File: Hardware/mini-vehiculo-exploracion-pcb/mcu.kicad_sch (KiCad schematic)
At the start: 19 parts, among them J2 USB_C_Receptacle_USB2.0_16P, SW1 SW_Push, SW2 SW_Push

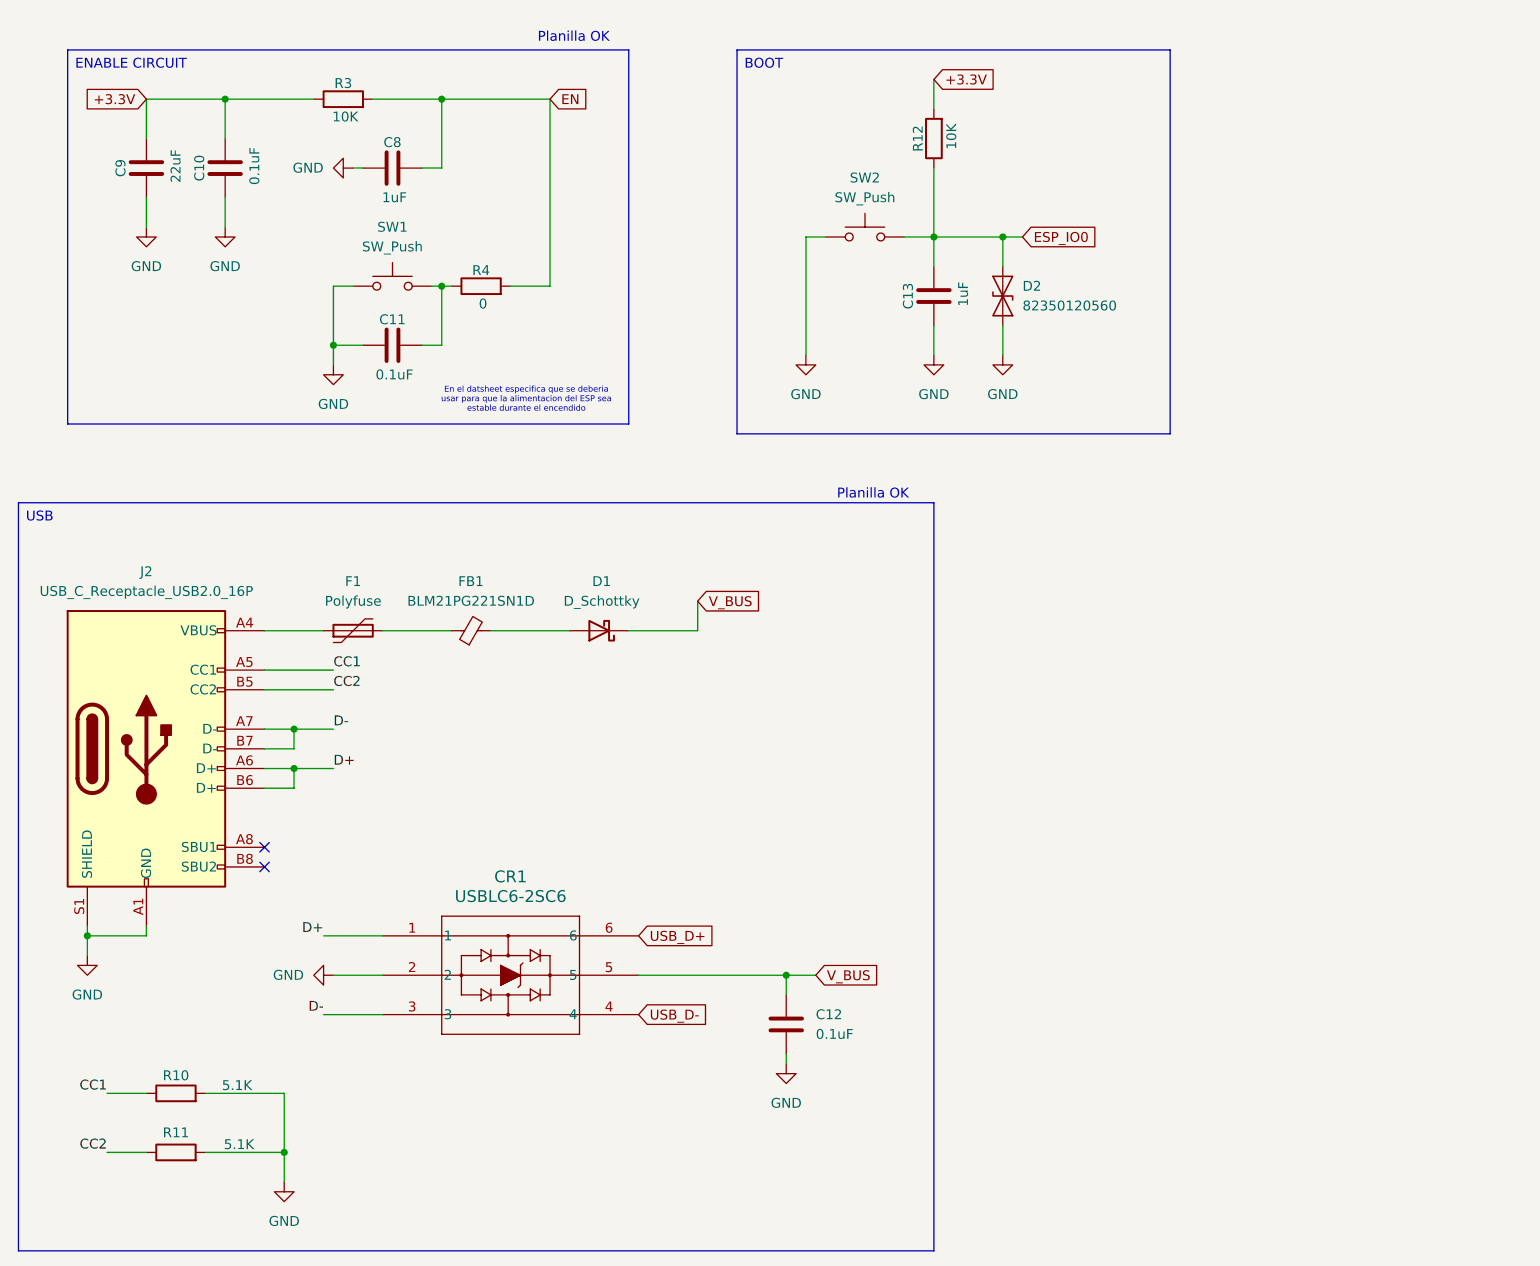
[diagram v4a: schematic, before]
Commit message: Add pin headers, run ERC
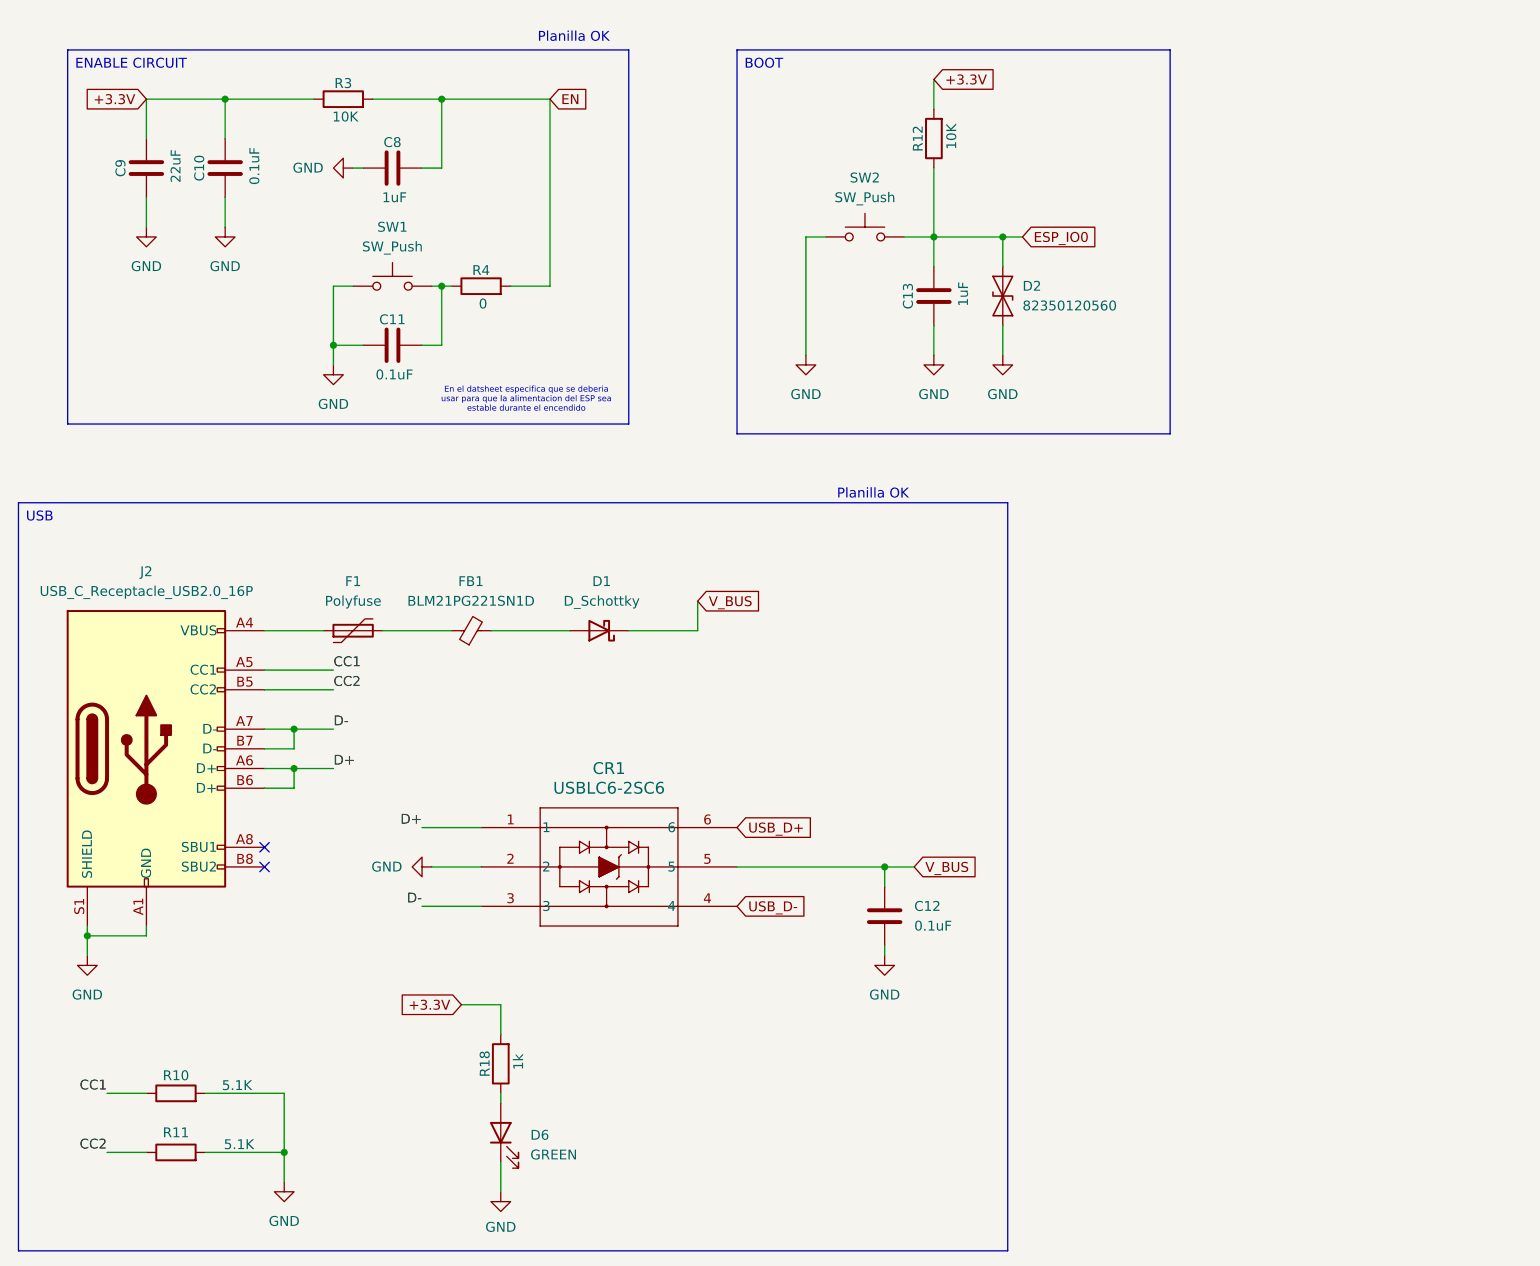
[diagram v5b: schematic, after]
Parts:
- added D6: GREEN, symbol Device:LED
- added R18: 1k, symbol Device:R
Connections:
- net +3.3V: now also R18.2
- net GND: now also D6.1 (K)
- new net: D6.2 (A), R18.1
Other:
- moved on the sheet: C12, CR1

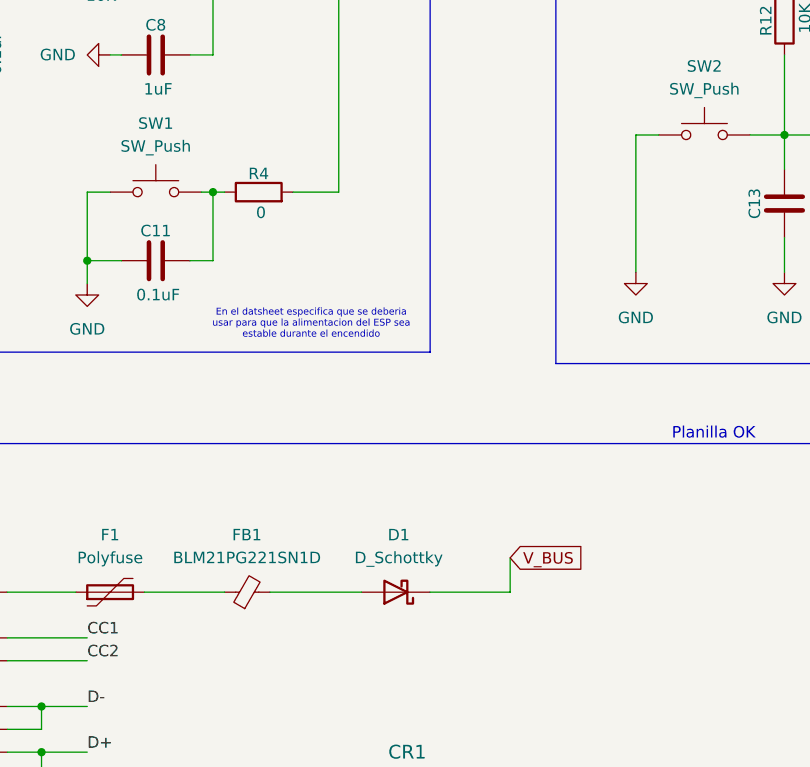
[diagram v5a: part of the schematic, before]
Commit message: Assigned NET CLASSES
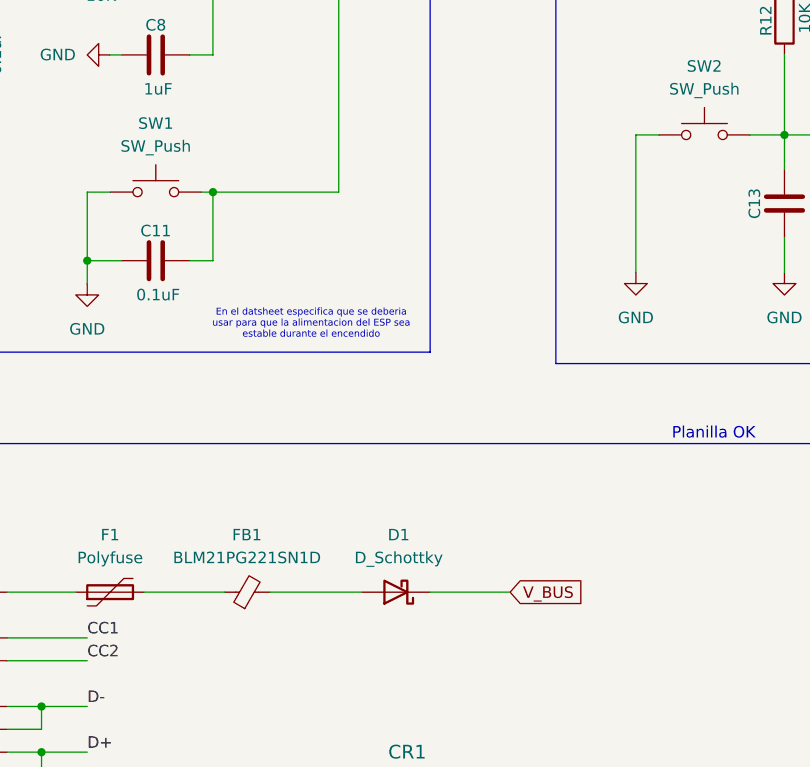
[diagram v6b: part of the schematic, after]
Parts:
- removed R4: 0, symbol Device:R
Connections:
- net EN: now also C11.2, SW1.2
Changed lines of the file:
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@@
-	(wire
-		(pts
-			(xy 110.49 101.6) (xy 110.49 97.79)
-		)
-		(stroke
-			(width 0)
-			(type default)
-		)
-	)
 	(wire
 		(pts
@@
 	(wire
 		(pts
-			(xy 86.36 57.15) (xy 91.44 57.15)
-		)
-		(stroke
-			(width 0)
-			(type default)
-		)
-	)
-	(wire
-		(pts
 			(xy 46.99 168.91) (xy 57.15 168.91)
 		)
@@
 	(wire
 		(pts
-			(xy 77.47 57.15) (xy 78.74 57.15)
+			(xy 77.47 57.15) (xy 91.44 57.15)
 		)
 		(stroke
@@
 	(global_label "V_BUS"
 		(shape input)
-		(at 110.49 97.79 0)
+		(at 110.49 101.6 0)
 		(fields_autoplaced yes)
 		(effects
@@
 		)
 		(property "Intersheetrefs" "${INTERSHEET_REFS}"
-			(at 119.3414 97.79 0)
+			(at 119.3414 101.6 0)
 			(effects
 				(font
@@
 					(unit 1)
 				)
-			)
-		)
-	)
-	(symbol
-		(lib_id "Device:R")
-		(at 82.55 57.15 90)
-		(unit 1)
-		(exclude_from_sim no)
-		(in_bom yes)
-		(on_board yes)
-		(dnp no)
-		(property "Reference" "R4"
-			(at 82.55 55.118 90)
-			(effects
-				(font
-					(size 1.27 1.27)
-				)
-			)
-		)
-		(property "Value" "0"
-			(at 82.804 59.436 90)
-			(effects
-				(font
-					(size 1.27 1.27)
-				)
-			)
-		)
-		(property "Footprint" ""
-			(at 82.55 58.928 90)
-			(effects
-				(font
-					(size 1.27 1.27)
-				)
-				(hide yes)
-			)
-		)
-		(property "Datasheet" "~"
-			(at 82.55 57.15 0)
-			(effects
-				(font
-					(size 1.27 1.27)
-				)
-				(hide yes)
-			)
-		)
-		(property "Description" "Resistor"
-			(at 82.55 57.15 0)
-			(effects
-				(font
-					(size 1.27 1.27)
-				)
-				(hide yes)
-			)
-		)
-		(pin "1"
-		)
-		(pin "2"
-		)
-		(instances
-			(project "mini-vehiculo-exploracion-pcb"
-				(path "/3cb3b833-c38f-47b4-b7e9-f0e6337b7613/7b198334-65f4-4536-9697-14ad78bccec0"
-					(reference "R4")
-					(unit 1)
-				)

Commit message: Add footprints
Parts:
- C10, C11, C12, C13, C8, C9: footprint (none) -> Capacitor_SMD:C_0805_2012Metric_Pad1.18x1.45mm_HandSolder
- D2: footprint (none) -> Diode_82350120560:CR_50120560_WRE-M
- D6: footprint (none) -> LED_SMD:LED_0805_2012Metric
- R10, R11, R12, R18, R3: footprint (none) -> Resistor_SMD:R_0805_2012Metric_Pad1.20x1.40mm_HandSolder
- SW1, SW2: footprint (none) -> B3FS-1010:B3FS-1000P
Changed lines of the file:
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@@
 			)
 		)
-		(property "Footprint" ""
+		(property "Footprint" "Resistor_SMD:R_0805_2012Metric_Pad1.20x1.40mm_HandSolder"
 			(at 43.18 170.688 90)
 			(effects
@@
 			)
 		)
-		(property "Footprint" ""
+		(property "Footprint" "Capacitor_SMD:C_0805_2012Metric_Pad1.18x1.45mm_HandSolder"
 			(at 38.4048 38.1 0)
 			(effects
@@
 			)
 		)
-		(property "Footprint" ""
+		(property "Footprint" "Capacitor_SMD:C_0805_2012Metric_Pad1.18x1.45mm_HandSolder"
 			(at 140.0048 54.61 0)
 			(effects
@@
 			)
 		)
-		(property "Footprint" ""
+		(property "Footprint" "Capacitor_SMD:C_0805_2012Metric_Pad1.18x1.45mm_HandSolder"
 			(at 135.5852 142.24 0)
 			(effects
@@
 			)
 		)
-		(property "Footprint" ""
+		(property "Footprint" "Capacitor_SMD:C_0805_2012Metric_Pad1.18x1.45mm_HandSolder"
 			(at 74.93 63.8048 0)
 			(effects
@@
 			)
 		)
-		(property "Footprint" ""
+		(property "Footprint" "Resistor_SMD:R_0805_2012Metric_Pad1.20x1.40mm_HandSolder"
 			(at 142.748 38.1 90)
 			(effects
@@
 			)
 		)
-		(property "Footprint" ""
+		(property "Footprint" "LED_SMD:LED_0805_2012Metric"
 			(at 85.09 166.37 0)
 			(effects
@@
 			)
 		)
-		(property "Footprint" ""
+		(property "Footprint" "B3FS-1010:B3FS-1000P"
 			(at 132.08 45.72 0)
 			(effects
@@
 			)
 		)
-		(property "Footprint" ""
+		(property "Footprint" "Capacitor_SMD:C_0805_2012Metric_Pad1.18x1.45mm_HandSolder"
 			(at 74.93 40.9448 0)
 			(effects
@@
 			)
 		)
-		(property "Footprint" ""
+		(property "Footprint" "Capacitor_SMD:C_0805_2012Metric_Pad1.18x1.45mm_HandSolder"
 			(at 48.5648 38.1 0)
 			(effects
@@
 			)
 		)
-		(property "Footprint" ""
+		(property "Footprint" "Diode_82350120560:CR_50120560_WRE-M"
 			(at 149.86 58.42 0)
 			(effects
@@
 			)
 		)
-		(property "Footprint" ""
+		(property "Footprint" "B3FS-1010:B3FS-1000P"
 			(at 71.12 52.07 0)
 			(effects
@@
 			)
 		)
-		(property "Footprint" ""
+		(property "Footprint" "Resistor_SMD:R_0805_2012Metric_Pad1.20x1.40mm_HandSolder"
 			(at 43.18 163.068 90)
 			(effects
@@
 			)
 		)
-		(property "Footprint" ""
+		(property "Footprint" "Resistor_SMD:R_0805_2012Metric_Pad1.20x1.40mm_HandSolder"
 			(at 64.77 34.798 90)
 			(effects
@@
 			)
 		)
-		(property "Footprint" ""
+		(property "Footprint" "Resistor_SMD:R_0805_2012Metric_Pad1.20x1.40mm_HandSolder"
 			(at 86.868 157.48 90)
 			(effects
